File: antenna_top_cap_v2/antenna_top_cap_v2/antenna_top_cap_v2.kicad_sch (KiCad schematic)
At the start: 55 parts, among them IC1 PCT2075DP,118, J1 Battery Charge Bypass, J10 BM04B-SRSS-TB(LF)(SN), J12 BM04B-SRSS-TB(LF)(SN), J14 BM04B-SRSS-TB(LF)(SN), J16 BM04B-SRSS-TB(LF)(SN), J19 Z+_Cap_Connector, J2 Conn_01x02, J3 Conn_01x02, J4 BM04B-SRSS-TB(LF)(SN)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

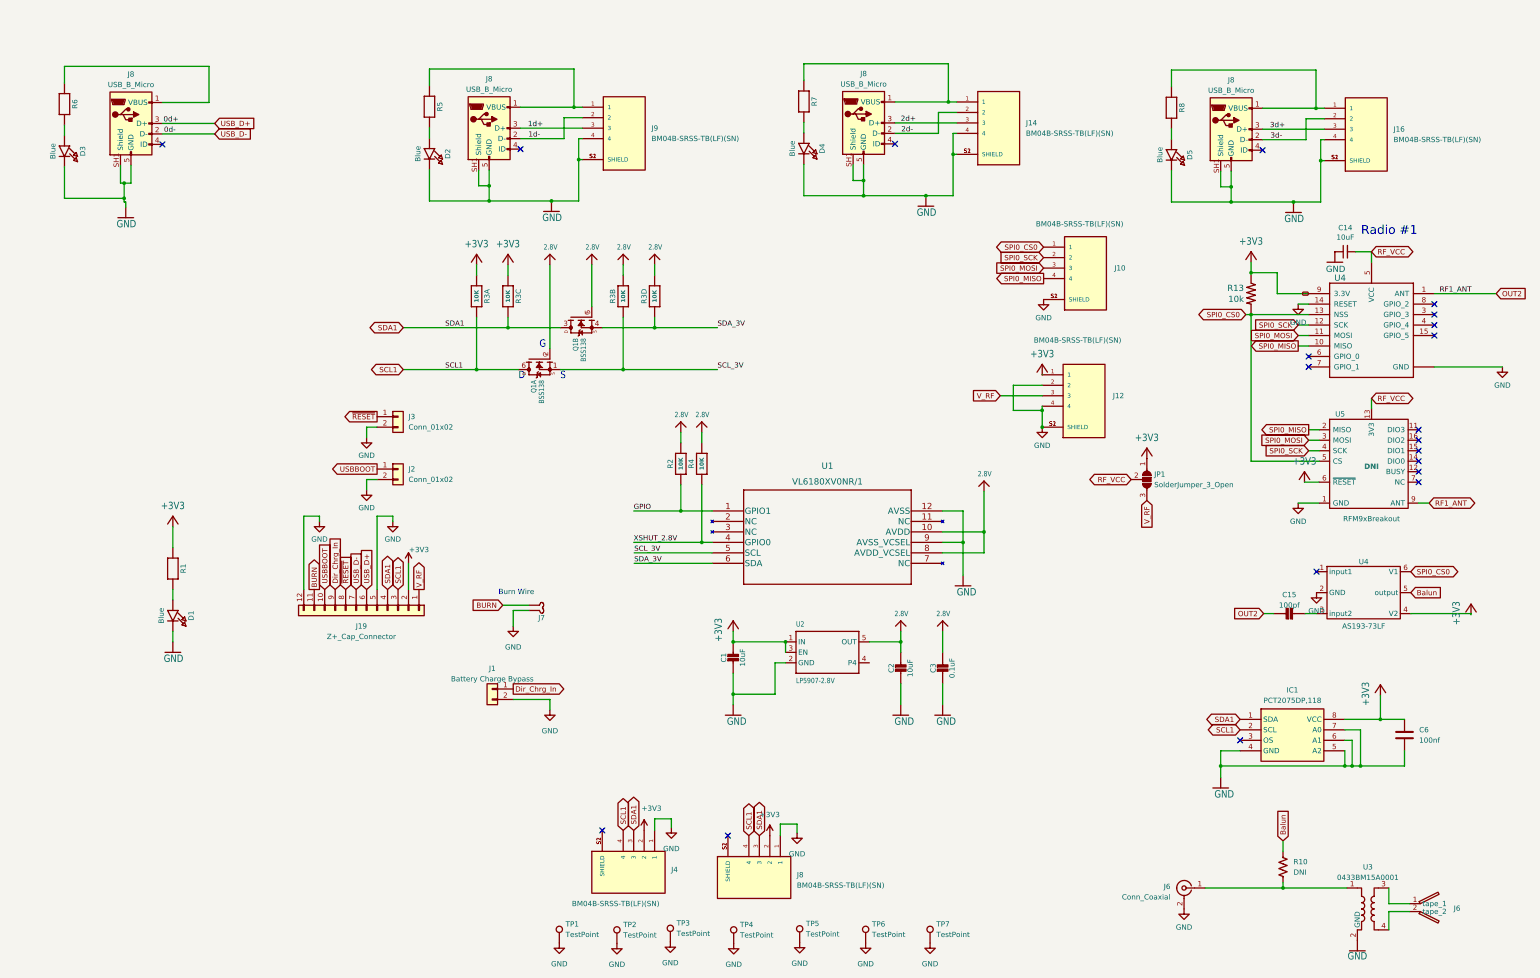
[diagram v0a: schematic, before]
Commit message: Schematic Updates and Renaming a Bunch of Files
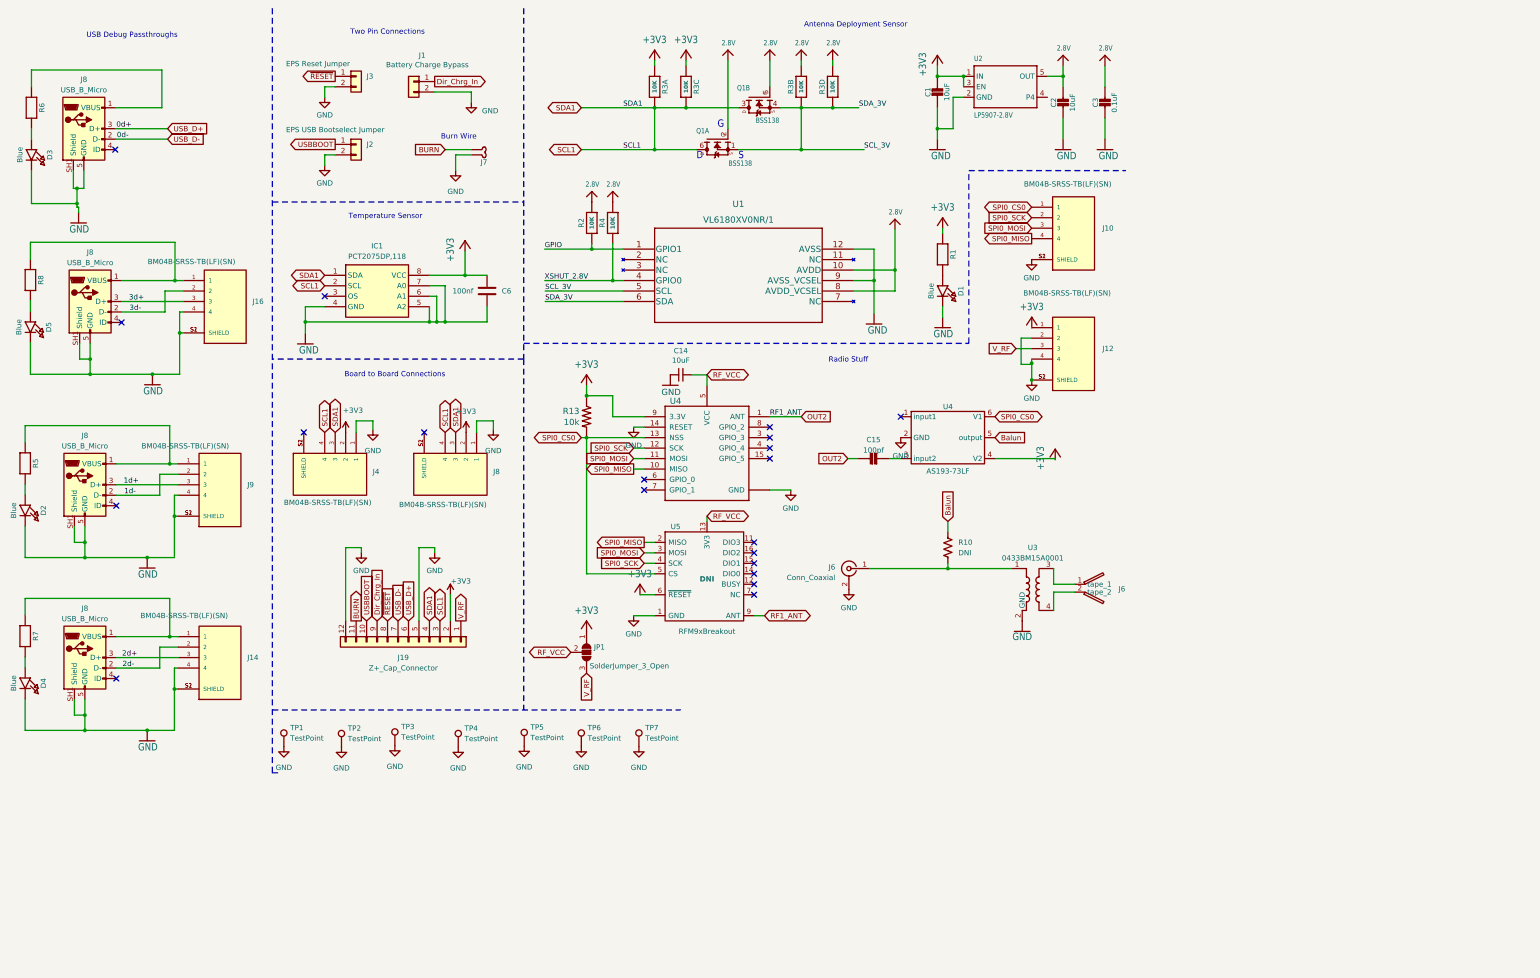
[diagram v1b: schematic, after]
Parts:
- J2: value Conn_01x02 -> EPS USB Bootselect Jumper
- J3: value Conn_01x02 -> EPS Reset Jumper
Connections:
- net SDA1 is gone; now on net SCL1: IC1.1 (SDA), J19.4 (Pin_4), J4.3, J8.3, Q1.3 (D), R3.6 (2)
- net SDA_3V is gone; now on net SCL_3V: Q1.4 (S), R3.5 (2), U1.6 (SDA)
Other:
- note added: "Antenna Deployment Sensor"
- note added: "Board to Board Connections"
- note added: "Radio Stuff"
- note added: "Temperature Sensor"
- note added: "Two Pin Connections"
- note added: "USB Debug Passthroughs"
- note removed: "Radio #1"
- moved on the sheet: C1, C14, C15, C2, C3, C6, D1, D2, D3, D4, D5, IC1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
